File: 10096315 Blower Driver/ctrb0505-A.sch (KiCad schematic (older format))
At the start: 133 parts, among them IC1 MotorDriver, IC2 NE555D, IC3 IR2118S, IC4 IR2118S, IC5 IR2118S, IC6 LinearRegulator, J1 2pinConnector_Power, J11 DNP, J2 10pinConnector, J22 DNP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

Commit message: Blower schematic: schematic and layout synchro
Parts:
- C1, C12, C15, C18, C19, C21, C24, C25, C26, C3, C5, C6, C9: footprint save10096315 Blower Driver:C0805 -> AllModules:C0805
- C10, C13, C16, R58, R59, R60: footprint save10096315 Blower Driver:RC1206 -> AllModules:RC1206
- C11, C14, C17, C20, C7, C8, FI3, FI4, FI5, FI6, FI7, FI8, FI9: footprint save10096315 Blower Driver:C0603 -> AllModules:C0603
- C2, C27: footprint save10096315 Blower Driver:03515 -> AllModules:03515
- C22, C23: footprint save10096315 Blower Driver:C0612-4 -> AllModules:C0612-4
- C28, C29: footprint save10096315 Blower Driver:HT-13X27 -> AllModules:HT-13X27
- C4: footprint save10096315 Blower Driver:C7343 -> AllModules:C7343
- D1, D18, D19, D20, D21, D22, D23: footprint save10096315 Blower Driver:SMB -> AllModules:SMB
- D10, D8, D9: footprint save10096315 Blower Driver:SMA -> AllModules:SMA
- D11, D12, D13: footprint save10096315 Blower Driver:SOD80 -> AllModules:SOD80
- D14, D15, D16, D24: footprint save10096315 Blower Driver:SOT23-1G -> AllModules:SOT23-1G
- D17: footprint save10096315 Blower Driver:DPAK-2ANODES -> AllModules:DPAK-2ANODES
- D2, D3, D4, D5, D6, D7: footprint save10096315 Blower Driver:SOD323 -> AllModules:SOD323
- F1: footprint save10096315 Blower Driver:FU154000 -> AllModules:FU154000
- FI1: footprint save10096315 Blower Driver:BNX002 -> AllModules:BNX002
- IC1: footprint save10096315 Blower Driver:MX.A24_COMPOSANT -> AllModules:MX.A24_COMPOSANT
- IC2, IC3, IC4, IC5: footprint save10096315 Blower Driver:MX.A8_COMPOSANT -> AllModules:MX.A8_COMPOSANT
- IC6: footprint save10096315 Blower Driver:DPAK -> AllModules:DPAK
- J1: footprint save10096315 Blower Driver:MOL43650-02C -> AllModules:MOL43650-02C
- J11: footprint save10096315 Blower Driver:MOL5566-2 -> AllModules:MOL5566-2
- J2: footprint save10096315 Blower Driver:BP2X5D -> AllModules:BP2X5D
- J22: footprint save10096315 Blower Driver:MOL7395-9 -> AllModules:MOL7395-9
- J3: footprint save10096315 Blower Driver:MOL7395-2 -> AllModules:MOL7395-2
- J6: footprint save10096315 Blower Driver:MOL7395-8 -> AllModules:MOL7395-8
- MIR1, MIR2, MIR3, MIR4: footprint save10096315 Blower Driver:MIRECMS-SAFT -> AllModules:MIRECMS-SAFT
- NT1: footprint AllModules:C12000_0 -> AllModules:NetTie-2_SMD_Pad0.5mm
- PT1: footprint save10096315 Blower Driver:C12000 -> AllModules:C12000
- R1, R40: footprint save10096315 Blower Driver:R2512 -> AllModules:R2512
- R10, R11, R12, R13, R2, R20, R3, R30, R31, R32, R33, R35, R37, R38, R39, R4, R41, R42, R5, R50, R6, R7, R8, R9: footprint save10096315 Blower Driver:R0603 -> AllModules:R0603
- T1, T10, T8: footprint save10096315 Blower Driver:SOT23-GSD -> AllModules:SOT23-GSD
- T2, T3, T4, T5, T6, T7, T9: footprint save10096315 Blower Driver:DPAK-GDS -> AllModules:DPAK-GDS
- ZC2: footprint save10096315 Blower Driver:C-SC8 -> AllModules:C-SC8
- ZC27: footprint save10096315 Blower Driver:C-SC10 -> AllModules:C-SC10
- ZT2, ZT3, ZT4, ZT5, ZT6, ZT7: footprint save10096315 Blower Driver:TO220ABGDS-INV_COUCHE -> AllModules:TO220ABGDS-INV_COUCHE

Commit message: Blower: library and project update from last pcb file
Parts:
- C2, C27: footprint AllModules:03515 -> AllModules:03515_10111101
- C28: footprint AllModules:HT-13X27 -> AllModules:HT-13X27_10111011
- C29: footprint AllModules:HT-13X27 -> AllModules:HT-13X27_10011011
- FI1: footprint AllModules:BNX002 -> AllModules:BNX002_101110011011101110111011
- J11: footprint AllModules:MOL5566-2 -> AllModules:MOL5566-2_10111011
- J2: footprint AllModules:BP2X5D -> AllModules:BP2X5D_1101100110111011101110011001100110111011
- J22: footprint AllModules:MOL7395-9 -> AllModules:MOL7395-9_110110011001100110011001100110011011
- J3: footprint AllModules:MOL7395-2 -> AllModules:MOL7395-2_10011001
- J4: footprint AllModules:JUMPER2_NoCopper_1 -> AllModules:JUMPER2_NoCopper
- J6: footprint AllModules:MOL7395-8 -> AllModules:MOL7395-8_10111011101110111101101110111011
- L1: footprint AllModules:ELC09DxxxxF_NoCopper_1 -> AllModules:ELC09DxxxxF_NoCopper
- NT1: footprint AllModules:NetTie-2_SMD_Pad0.5mm -> AllModules:NetTie-2_SMD_Pad_2.5x5mm
- ZM1, ZM2, ZM3, ZM4: footprint AllModules:FIX35M -> AllModules:FIX35M_1101
- ZT2, ZT4, ZT6: footprint AllModules:TO220ABGDS-INV_COUCHE -> AllModules:TO220ABGDS-INV_COUCHE_101110011001
- ZT3, ZT5, ZT7: footprint AllModules:TO220ABGDS-INV_COUCHE -> AllModules:TO220ABGDS-INV_COUCHE_101110011011
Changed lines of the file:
@@
 F 0 "FI1" H 2650 2650 50  0000 C CNN
 F 1 "DNP" H 2650 2550 50  0000 C CNN
-F 2 "AllModules:BNX002" H 2500 2600 50  0001 C CNN
+F 2 "AllModules:BNX002_101110011011101110111011" H 2500 2600 50  0001 C CNN
 F 3 "" H 2500 2600 50  0001 C CNN
 F 4 "FILTER CC, 1MHZ-1GHZ, 10A, 50V" H 2800 2300 50  0001 C CNN "Description"
@@
 F 0 "L1" V 2850 1225 50  0000 C CNN
 F 1 "22uH" V 2925 1275 50  0000 C CNN
-F 2 "AllModules:ELC09DxxxxF_NoCopper_1" H 3050 1700 50  0001 C CNN
+F 2 "AllModules:ELC09DxxxxF_NoCopper" H 3050 1700 50  0001 C CNN
 F 3 "" H 3050 1700 50  0001 C CNN
 F 4 "INDUCTOR 22UH,1.8-2A" H 3050 1700 50  0001 C CNN "Description"
@@
 F 0 "J4" V 2400 2850 50  0000 C CNN
 F 1 "JumperBypass" V 2500 2850 50  0000 C CNN
-F 2 "AllModules:JUMPER2_NoCopper_1" H 2700 3350 50  0001 C CNN
+F 2 "AllModules:JUMPER2_NoCopper" H 2700 3350 50  0001 C CNN
 F 3 "" H 2700 3350 50  0001 C CNN
 F 4 "COPPER WIRE, SWG20 DIA: 0.91" H 2700 2850 50  0001 C CNN "Description"
@@
 F 0 "J11" H 1300 2550 50  0000 C CNN
 F 1 "DNP" H 1350 2250 50  0000 C CNN
-F 2 "AllModules:MOL5566-2" H 1400 2600 50  0001 C CNN
+F 2 "AllModules:MOL5566-2_10111011" H 1400 2600 50  0001 C CNN
 F 3 "https://www.molex.com/pdm_docs/sd/039281023_sd.pdf" H 1400 2600 50  0001 C CNN
 F 4 " CONN HEADER VERT 2 CONTACTS Mini Fit Jr  5.5PIN PITCH" H 1400 2600 50  0001 C CNN "Description"
@@
 F 0 "J6" H 21525 7600 50  0000 R CNN
 F 1 "8pinConnector" H 21625 6650 50  0000 R CNN
-F 2 "AllModules:MOL7395-8" H 21625 7650 50  0001 C CNN
+F 2 "AllModules:MOL7395-8_10111011101110111101101110111011" H 21625 7650 50  0001 C CNN
 F 3 "" H 21625 7650 50  0001 C CNN
 F 4 "CONNECTOR,8 CONTACTS, 2.54PIN PITCH" H 21575 7150 50  0001 C CNN "Description"
@@
 F 0 "J3" H 21525 6050 50  0000 R CNN
 F 1 "2pinConnector" H 21625 5700 50  0000 R CNN
-F 2 "AllModules:MOL7395-2" H 21625 6150 50  0001 C CNN
+F 2 "AllModules:MOL7395-2_10011001" H 21625 6150 50  0001 C CNN
 F 3 "" H 21625 6150 50  0001 C CNN
 F 4 "CONNECTOR, O2 VALVE, 2 CONTACTS" H 21575 5900 50  0001 C CNN "Description"
@@
 F 0 "J2" H 1600 13150 50  0000 C CNN
 F 1 "10pinConnector" H 1500 13250 50  0000 C CNN
-F 2 "AllModules:BP2X5D" H 1800 13200 50  0001 C CNN
+F 2 "AllModules:BP2X5D_1101100110111011101110011001100110111011" H 1800 13200 50  0001 C CNN
 F 3 "" H 1800 13200 50  0001 C CNN
 F 4 "PCB CONNECTOR HE10, 10 PINS" H 1750 12700 50  0001 C CNN "Description"
@@
 F 0 "C28" H 16340 2491 50  0000 L CNN
 F 1 "1000uF" H 16475 2400 50  0000 C CNN
-F 2 "AllModules:HT-13X27" H 16275 1950 50  0001 C CNN
+F 2 "AllModules:HT-13X27_10111011" H 16275 1950 50  0001 C CNN
 F 3 "" H 16225 2850 50  0001 C CNN
 F 4 "CAPACITOR,1000UF,+/-20%,35V" H 16225 2400 50  0001 C CNN "Description"
@@
 F 0 "C29" H 17040 2491 50  0000 L CNN
 F 1 "1000uF" H 17175 2400 50  0000 C CNN
-F 2 "AllModules:HT-13X27" H 16975 1950 50  0001 C CNN
+F 2 "AllModules:HT-13X27_10011011" H 16975 1950 50  0001 C CNN
 F 3 "" H 16925 2850 50  0001 C CNN
 F 4 "CAPACITOR,1000UF,+/-20%,35V" H 16925 2400 50  0001 C CNN "Description"
@@
 F 0 "NT1" H 10450 13000 50  0000 C CNN
 F 1 "Net-Tie_2" H 10450 12800 50  0000 C CNN
-F 2 "AllModules:NetTie-2_SMD_Pad0.5mm" H 10450 12900 50  0001 C CNN
+F 2 "AllModules:NetTie-2_SMD_Pad_2.5x5mm" H 10450 12900 50  0001 C CNN
 F 3 "" H 10450 12900 50  0001 C CNN
 	1    10450 12900
@@
 F 0 "ZM4" H 4100 6599 50  0000 L CNN
 F 1 "MountingHole_Pad" H 4100 6508 50  0000 L CNN
-F 2 "AllModules:FIX35M" H 4000 6550 50  0001 C CNN
+F 2 "AllModules:FIX35M_1101" H 4000 6550 50  0001 C CNN
 F 3 "~" H 4000 6550 50  0001 C CNN
 	1    4000 6550
@@
 F 0 "ZM3" H 5100 6599 50  0000 L CNN
 F 1 "MountingHole_Pad" H 5100 6508 50  0000 L CNN
-F 2 "AllModules:FIX35M" H 5000 6550 50  0001 C CNN
+F 2 "AllModules:FIX35M_1101" H 5000 6550 50  0001 C CNN
 F 3 "~" H 5000 6550 50  0001 C CNN
 	1    5000 6550
@@
 F 0 "ZM1" H 4100 7099 50  0000 L CNN
 F 1 "MountingHole_Pad" H 4100 7008 50  0000 L CNN
-F 2 "AllModules:FIX35M" H 4000 7050 50  0001 C CNN
+F 2 "AllModules:FIX35M_1101" H 4000 7050 50  0001 C CNN
 F 3 "~" H 4000 7050 50  0001 C CNN
 	1    4000 7050
@@
 F 0 "ZM2" H 5100 7099 50  0000 L CNN
 F 1 "MountingHole_Pad" H 5100 7008 50  0000 L CNN
-F 2 "AllModules:FIX35M" H 5000 7050 50  0001 C CNN
+F 2 "AllModules:FIX35M_1101" H 5000 7050 50  0001 C CNN
 F 3 "~" H 5000 7050 50  0001 C CNN
 	1    5000 7050
@@
 F 0 "J22" H 1708 10075 50  0000 C CNN
 F 1 "DNP" H 1708 9984 50  0000 C CNN
-F 2 "AllModules:MOL7395-9" H 1800 10150 50  0001 C CNN
+F 2 "AllModules:MOL7395-9_110110011001100110011001100110011011" H 1800 10150 50  0001 C CNN
 F 3 "https://www.molex.com/webdocs/datasheets/pdf/en-us/0022057098_PCB_HEADERS.pdf" H 1800 10150 50  0001 C CNN
 F 4 "Molex" H 0   0   50  0001 C CNN "Manufacturer"
@@
 F 0 "C27" H 11275 2500 50  0000 L CNN
 F 1 "DNP" H 11150 2850 50  0001 C CNN
-F 2 "AllModules:03515" H 11200 1950 50  0001 C CNN
+F 2 "AllModules:03515_10111101" H 11200 1950 50  0001 C CNN
 F 3 "https://industrial.panasonic.com/ww/products/capacitors/aluminum-capacitors/aluminum-cap-lead/models/ECA1EHG471B" H 11150 2850 50  0001 C CNN
 F 4 "CAPACITOR,470UF, +/-20%,25V TH" H 11150 2400 50  0001 C CNN "Description"
@@
 F 0 "ZT2" H 19275 4200 50  0000 L CNN
 F 1 "DNP" H 19225 4550 50  0001 C CNN
-F 2 "AllModules:TO220ABGDS-INV_COUCHE" H 19275 3400 50  0001 C CNN
+F 2 "AllModules:TO220ABGDS-INV_COUCHE_101110011001" H 19275 3400 50  0001 C CNN
 F 3 "http://www.vishay.com/docs/91406/sihfz24.pdf" H 19225 4450 50  0001 C CNN
 F 4 "TRANSISTOR MOSFET, 60V, 16.7A,  N CHANNEL" H 19225 4050 50  0001 C CNN "Description"
@@
 F 0 "ZT3" H 19275 4800 50  0000 L CNN
 F 1 "DNP" H 19225 5150 50  0001 C CNN
-F 2 "AllModules:TO220ABGDS-INV_COUCHE" H 19275 4000 50  0001 C CNN
+F 2 "AllModules:TO220ABGDS-INV_COUCHE_101110011011" H 19275 4000 50  0001 C CNN
 F 3 "http://www.vishay.com/docs/91406/sihfz24.pdf" H 19225 5050 50  0001 C CNN
 F 4 "TRANSISTOR MOSFET, 60V, 16.7A,  N CHANNEL" H 19225 4650 50  0001 C CNN "Description"
@@
 F 0 "ZT4" H 19275 7000 50  0000 L CNN
 F 1 "DNP" H 19225 7350 50  0001 C CNN
-F 2 "AllModules:TO220ABGDS-INV_COUCHE" H 19275 6200 50  0001 C CNN
+F 2 "AllModules:TO220ABGDS-INV_COUCHE_101110011001" H 19275 6200 50  0001 C CNN
 F 3 "http://www.vishay.com/docs/91406/sihfz24.pdf" H 19225 7250 50  0001 C CNN
 F 4 "TRANSISTOR MOSFET, 60V, 16.7A,  N CHANNEL" H 19225 6850 50  0001 C CNN "Description"
@@
 F 0 "ZT5" H 19275 7600 50  0000 L CNN
 F 1 "DNP" H 19225 7950 50  0001 C CNN
-F 2 "AllModules:TO220ABGDS-INV_COUCHE" H 19275 6800 50  0001 C CNN
+F 2 "AllModules:TO220ABGDS-INV_COUCHE_101110011011" H 19275 6800 50  0001 C CNN
 F 3 "http://www.vishay.com/docs/91406/sihfz24.pdf" H 19225 7850 50  0001 C CNN
 F 4 "TRANSISTOR MOSFET, 60V, 16.7A,  N CHANNEL" H 19225 7450 50  0001 C CNN "Description"
@@
 F 0 "ZT6" H 19275 9900 50  0000 L CNN
 F 1 "DNP" H 19225 10250 50  0001 C CNN
-F 2 "AllModules:TO220ABGDS-INV_COUCHE" H 19275 9100 50  0001 C CNN
+F 2 "AllModules:TO220ABGDS-INV_COUCHE_101110011001" H 19275 9100 50  0001 C CNN
 F 3 "http://www.vishay.com/docs/91406/sihfz24.pdf" H 19225 10150 50  0001 C CNN
 F 4 "TRANSISTOR MOSFET, 60V, 16.7A,  N CHANNEL" H 19225 9750 50  0001 C CNN "Description"
@@
 F 0 "ZT7" H 19275 10500 50  0000 L CNN
 F 1 "DNP" H 19225 10850 50  0001 C CNN
-F 2 "AllModules:TO220ABGDS-INV_COUCHE" H 19275 9700 50  0001 C CNN
+F 2 "AllModules:TO220ABGDS-INV_COUCHE_101110011011" H 19275 9700 50  0001 C CNN
 F 3 "http://www.vishay.com/docs/91406/sihfz24.pdf" H 19225 10750 50  0001 C CNN
 F 4 "TRANSISTOR MOSFET, 60V, 16.7A,  N CHANNEL" H 19225 10350 50  0001 C CNN "Description"
@@
 F 0 "C2" H 8916 2484 50  0000 L CNN
 F 1 "100uF" H 8800 2850 50  0001 C CNN
-F 2 "AllModules:03515" H 8850 1950 50  0001 C CNN
+F 2 "AllModules:03515_10111101" H 8850 1950 50  0001 C CNN
 F 3 "" H 8800 2850 50  0001 C CNN
 F 4 "10022506_TH" H 8800 2400 50  0001 C CNN "Item Number"

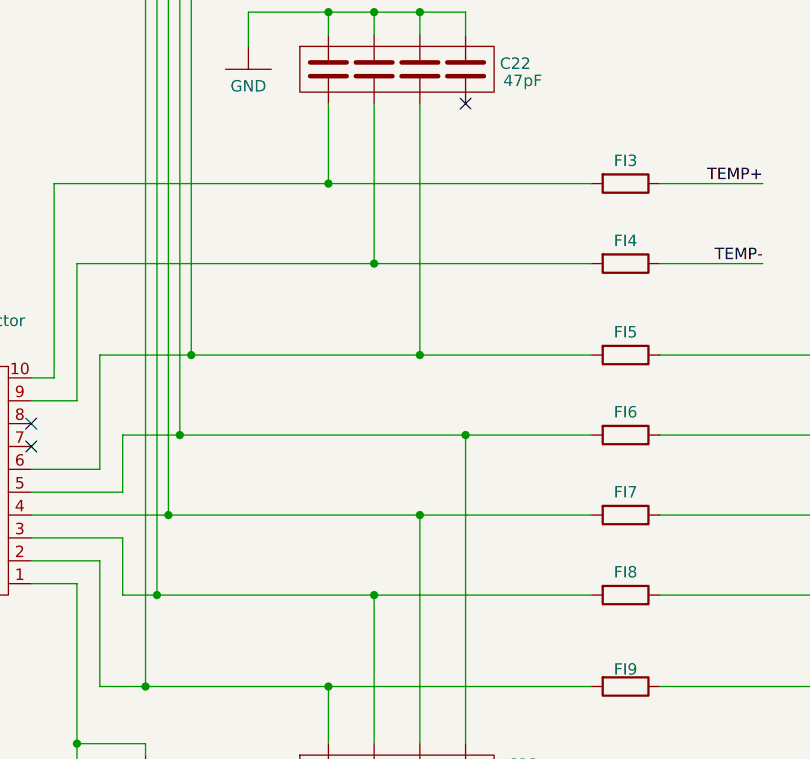
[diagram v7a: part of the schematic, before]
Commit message: Rename net names on schematics
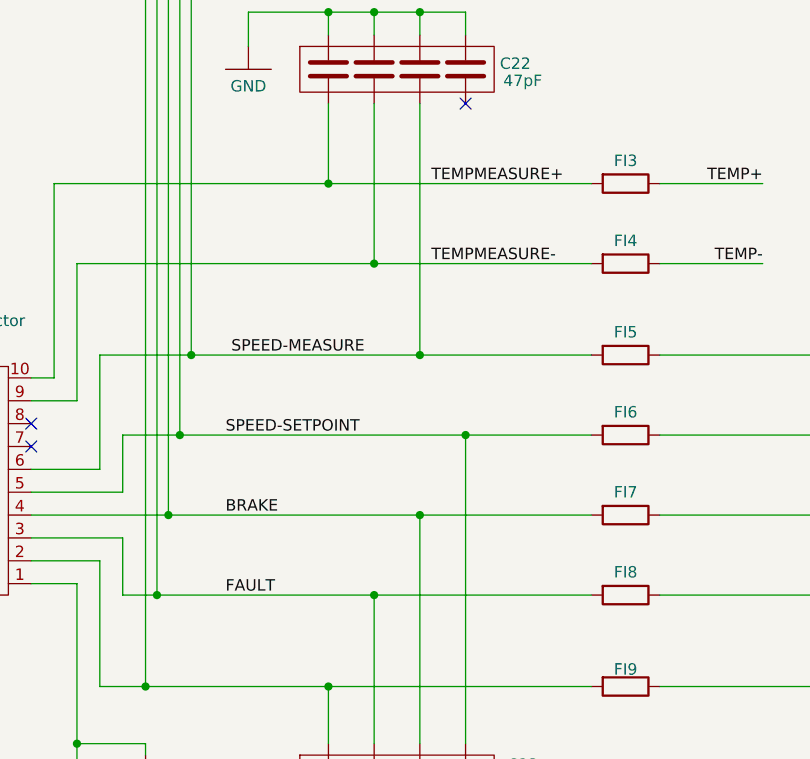
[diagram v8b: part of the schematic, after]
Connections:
- net TEMPMEASURE+: now reaches C22.1, FI3.1, J2.10
- net TEMPMEASURE-: now reaches C22.2, FI4.1, J2.9
- net SPEED-MEASURE: now reaches C22.3, FI5.1, J2.6, J22.6
- net SPEED-SETPOINT: now reaches C23.5, FI6.1, J2.5, J22.5
- net BRAKE: now reaches C23.6, FI7.1, J2.4, J22.4
- net FAULT: now reaches C23.7, FI8.1, J2.3, J22.3
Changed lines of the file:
@@
 F1 "ctrb0505-B.sch" 50
 $EndSheet
+Text Label 3550 11550 0    50   ~ 0
+TEMPMEASURE+
+Text Label 3550 11900 0    50   ~ 0
+TEMPMEASURE-
+Text Label 2650 12650 0    50   ~ 0
+SPEED-SETPOINT
+Text Label 2650 13000 0    50   ~ 0
+BRAKE
+Text Label 2650 13350 0    50   ~ 0
+FAULT
+Text Label 2675 12300 0    50   ~ 0
+SPEED-MEASURE
 $EndSCHEMATC
